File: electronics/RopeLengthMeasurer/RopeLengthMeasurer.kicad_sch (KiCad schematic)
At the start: 13 parts

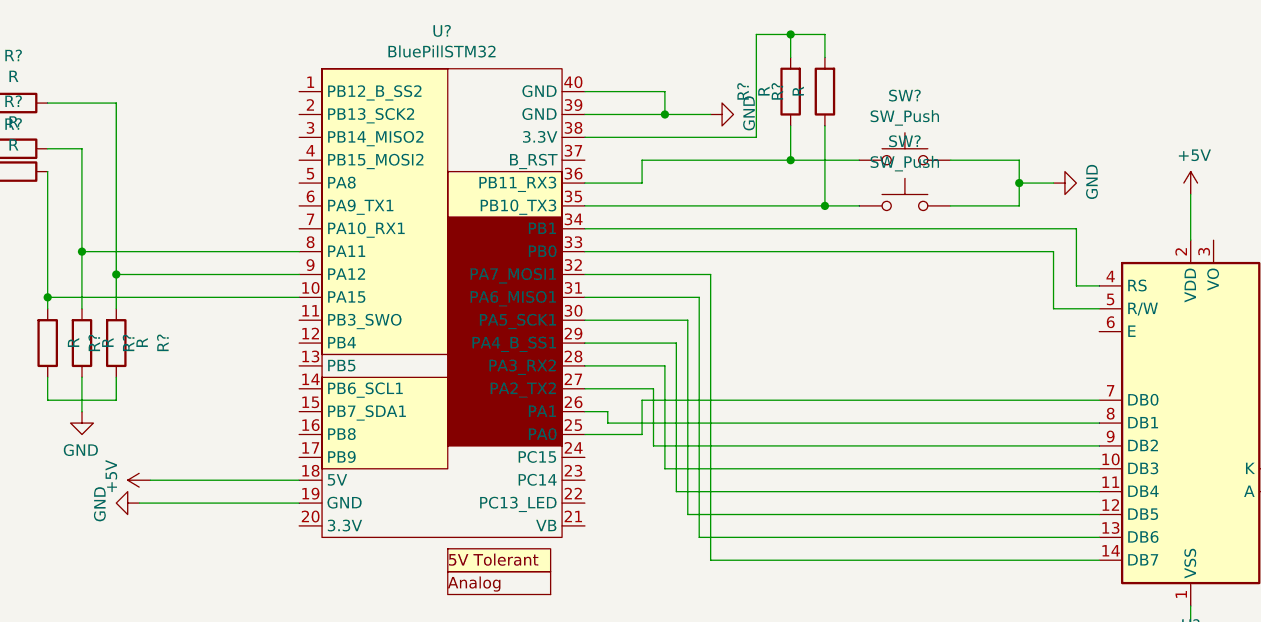
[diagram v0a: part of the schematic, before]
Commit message: Switching design to black pill.
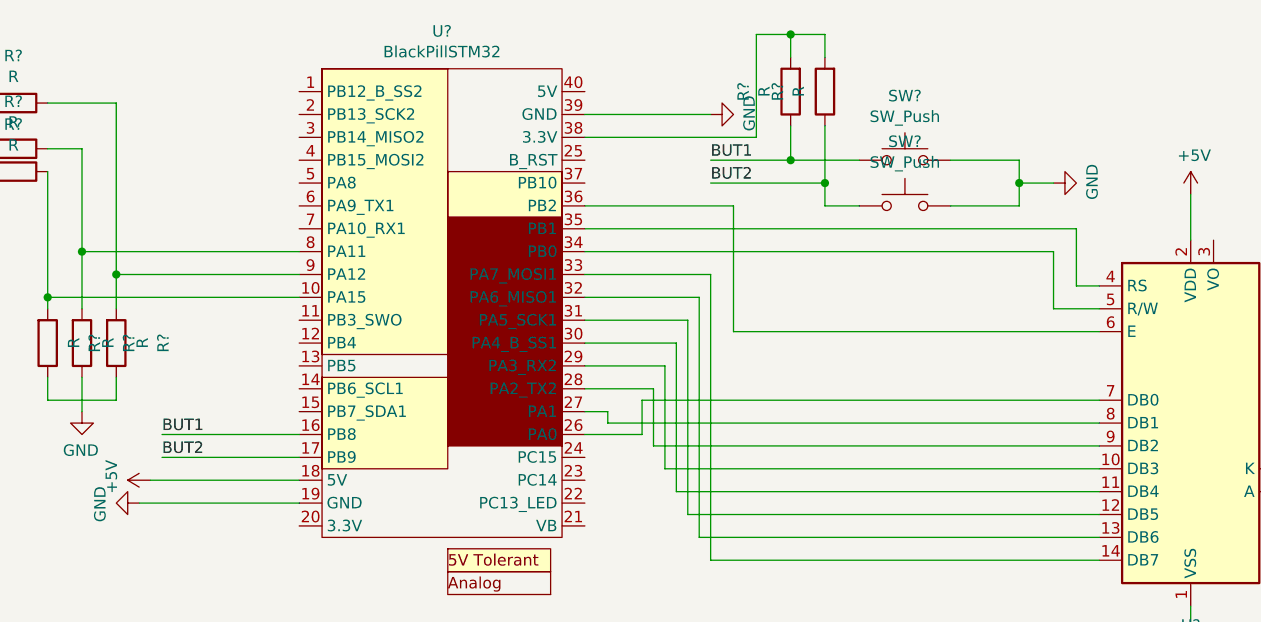
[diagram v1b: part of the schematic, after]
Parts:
- removed U?: BluePillSTM32, symbol RopeLengthMeasurerLibrary:BluePillSTM32
- added U?: BlackPillSTM32, symbol RopeLengthMeasurerLibrary:BlackPillSTM32
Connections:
- net +5V: now also U?.18 (5V)
- net GND: now also U?.19 (GND), U?.39 (GND)
- net at R?.1, R?.2: now also U?.8 (PA11)
- net at R?.1, R?.2: now also U?.10 (PA15)
- net at U?.7 (DB0): now also U?.26 (PA0)
- net at U?.8 (DB1): now also U?.27 (PA1)
- net at U?.9 (DB2): now also U?.28 (PA2_TX2)
- net at U?.10 (DB3): now also U?.29 (PA3_RX2)
- net at U?.11 (DB4): now also U?.30 (PA4_B_SS1)
- net at U?.12 (DB5): now also U?.31 (PA5_SCK1)
- net at U?.13 (DB6): now also U?.32 (PA6_MISO1)
- net at U?.14 (DB7): now also U?.33 (PA7_MOSI1)
- net at U?.5 (R/W): now also U?.34 (PB0)
- net at U?.4 (RS): now also U?.35 (PB1)
- net BUT2: now reaches R?.1, SW?.1
- net BUT2: now also U?.17 (PB9)
- net BUT1: now reaches R?.1, SW?.1
- net BUT1: now also U?.16 (PB8)
- net at R?.2, R?.2: now also U?.38 (3.3V)
- net at R?.1, R?.2: now also U?.9 (PA12)
- net at U?.6 (E): now also U?.36 (PB2)
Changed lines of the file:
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@@
     (title "Rope Length Measurer")
   )
+  (junction (at 180.34 92.71))
+  (junction (at 180.34 106.68))
   (junction (at 205.74 109.22))
-  (junction (at 184.15 111.76))
-  (junction (at 180.34 106.68))
   (junction (at 97.79 121.92))
-  (junction (at 180.34 92.71))
-  (junction (at 166.37 101.6))
   (junction (at 101.6 116.84))
   (junction (at 105.41 119.38))
+  (junction (at 184.15 109.22))
   (wire (pts (xy 81.28 110.49) (xy 78.74 110.49)))
   (wire (pts (xy 81.28 113.03) (xy 81.28 110.49)))
@@
   (wire (pts (xy 107.95 144.78) (xy 125.73 144.78)))
   (wire (pts (xy 109.22 142.24) (xy 125.73 142.24)))
-  (wire (pts (xy 157.48 99.06) (xy 166.37 99.06)))
-  (wire (pts (xy 157.48 101.6) (xy 166.37 101.6)))
+  (wire (pts (xy 110.49 137.16) (xy 125.73 137.16)))
+  (wire (pts (xy 110.49 139.7) (xy 125.73 139.7)))
+  (wire (pts (xy 157.48 101.6) (xy 171.45 101.6)))
   (wire (pts (xy 157.48 104.14) (xy 176.53 104.14)))
-  (wire (pts (xy 157.48 109.22) (xy 163.83 109.22)))
-  (wire (pts (xy 157.48 111.76) (xy 184.15 111.76)))
+  (wire (pts (xy 157.48 111.76) (xy 173.99 111.76)))
   (wire (pts (xy 157.48 114.3) (xy 212.09 114.3)))
   (wire (pts (xy 157.48 134.62) (xy 160.02 134.62)))
   (wire (pts (xy 160.02 134.62) (xy 160.02 135.89)))
   (wire (pts (xy 160.02 135.89) (xy 214.63 135.89)))
-  (wire (pts (xy 163.83 106.68) (xy 180.34 106.68)))
-  (wire (pts (xy 163.83 109.22) (xy 163.83 106.68)))
   (wire (pts (xy 163.83 133.35) (xy 163.83 137.16)))
   (wire (pts (xy 163.83 137.16) (xy 157.48 137.16)))
   (wire (pts (xy 165.1 132.08) (xy 157.48 132.08)))
   (wire (pts (xy 165.1 138.43) (xy 165.1 132.08)))
-  (wire (pts (xy 166.37 101.6) (xy 166.37 99.06)))
-  (wire (pts (xy 166.37 101.6) (xy 171.45 101.6)))
   (wire (pts (xy 166.37 129.54) (xy 157.48 129.54)))
   (wire (pts (xy 166.37 140.97) (xy 166.37 129.54)))
@@
   (wire (pts (xy 170.18 121.92) (xy 157.48 121.92)))
   (wire (pts (xy 170.18 148.59) (xy 170.18 121.92)))
+  (wire (pts (xy 171.45 106.68) (xy 180.34 106.68)))
+  (wire (pts (xy 171.45 109.22) (xy 184.15 109.22)))
   (wire (pts (xy 171.45 119.38) (xy 157.48 119.38)))
   (wire (pts (xy 171.45 151.13) (xy 171.45 119.38)))
+  (wire (pts (xy 173.99 111.76) (xy 173.99 125.73)))
+  (wire (pts (xy 173.99 125.73) (xy 214.63 125.73)))
   (wire (pts (xy 176.53 92.71) (xy 180.34 92.71)))
   (wire (pts (xy 176.53 104.14) (xy 176.53 92.71)))
@@
   (wire (pts (xy 180.34 106.68) (xy 187.96 106.68)))
   (wire (pts (xy 184.15 92.71) (xy 184.15 95.25)))
-  (wire (pts (xy 184.15 102.87) (xy 184.15 111.76)))
+  (wire (pts (xy 184.15 102.87) (xy 184.15 109.22)))
+  (wire (pts (xy 184.15 109.22) (xy 184.15 111.76)))
   (wire (pts (xy 184.15 111.76) (xy 187.96 111.76)))
   (wire (pts (xy 198.12 106.68) (xy 205.74 106.68)))
@@
   (wire (pts (xy 224.79 110.49) (xy 224.79 115.57)))
   (wire (pts (xy 224.79 156.21) (xy 224.79 161.29)))
+  (label "BUT1" (at 110.49 137.16 0)
+    (effects (font (size 1.27 1.27)) (justify left bottom))
+  )
+  (label "BUT2" (at 110.49 139.7 0)
+    (effects (font (size 1.27 1.27)) (justify left bottom))
+  )
+  (label "BUT1" (at 171.45 106.68 0)
+    (effects (font (size 1.27 1.27)) (justify left bottom))
+  )
+  (label "BUT2" (at 171.45 109.22 0)
+    (effects (font (size 1.27 1.27)) (justify left bottom))
+  )
   (symbol (lib_id "power:+5V") (at 88.9 96.52 0) (mirror y) (unit 1)
     (property "Reference" "#PWR?" (id 0) (at 88.9 100.33 0)
@@
     )
   )
-  (symbol (lib_id "RopeLengthMeasurerLibrary:BluePillSTM32") (at 140.97 125.73 0) (unit 1)
+  (symbol (lib_id "RopeLengthMeasurerLibrary:BlackPillSTM32") (at 140.97 125.73 0) (unit 1)
     (property "Reference" "U?" (id 0) (at 141.605 92.3606 0))
-    (property "Value" "BluePillSTM32" (id 1) (at 141.605 94.6593 0))
+    (property "Value" "BlackPillSTM32" (id 1) (at 141.605 94.6593 0))
     (property "Footprint" "" (id 2) (at 140.97 125.73 0)
       (effects (font (size 1.27 1.27)) hide)
@@
     (path "/7277fe0f-8eb6-42d9-9146-42338237283f" (reference "SW?") (unit 1))
     (path "/8c9fb5c0-6949-4714-a6e4-1cb24319bb3d" (reference "SW?") (unit 1))
-    (path "/363120c1-d9a0-48f5-bc66-fe3ce3559d16" (reference "U?") (unit 1))
+    (path "/3ffa81b3-2fad-40d0-843d-3ea2c963161d" (reference "U?") (unit 1))
     (path "/4f978266-5538-4d2e-ab75-02c33b1c508d" (reference "U?") (unit 1))
     (path "/91db2f3c-0f8a-4d8d-8519-75a14ded5ae0" (reference "U?") (unit 1))

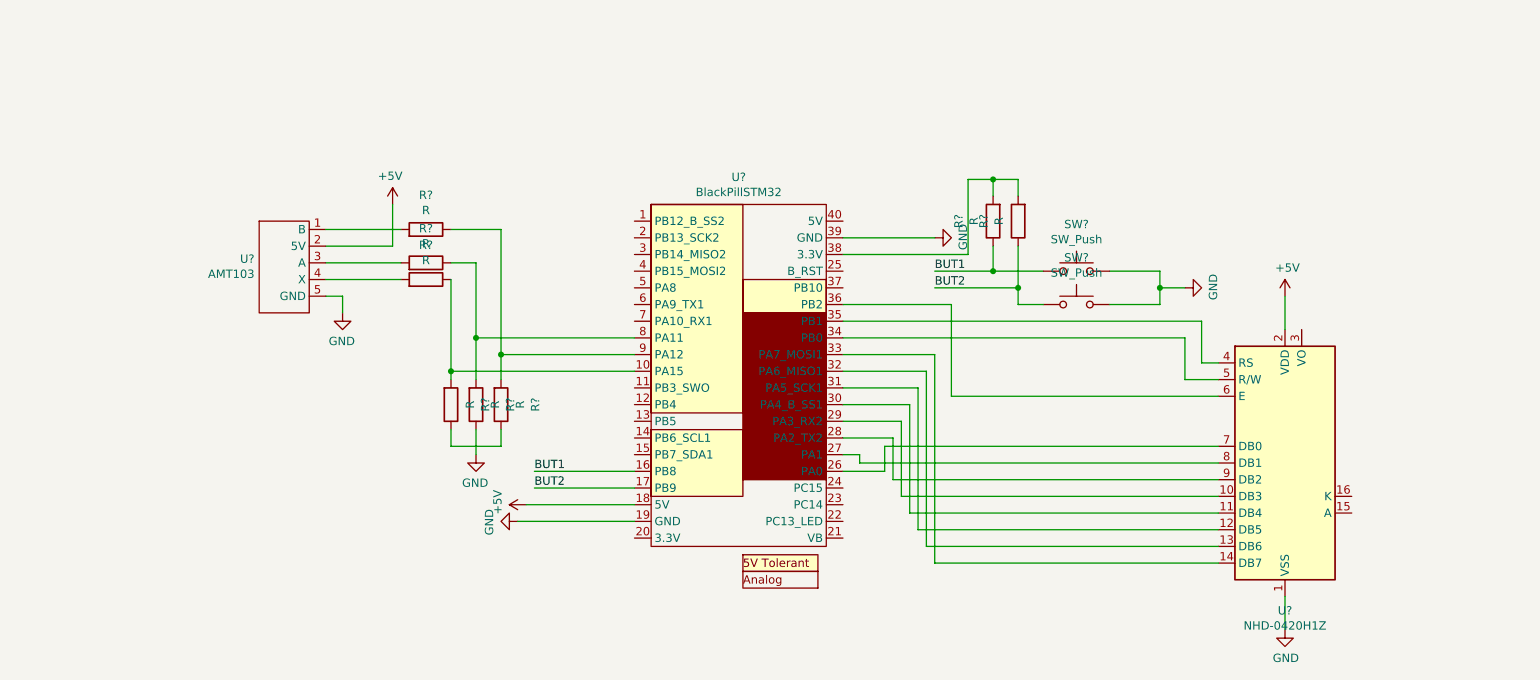
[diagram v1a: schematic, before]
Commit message: Software working with new circuit board. Reset button also working.
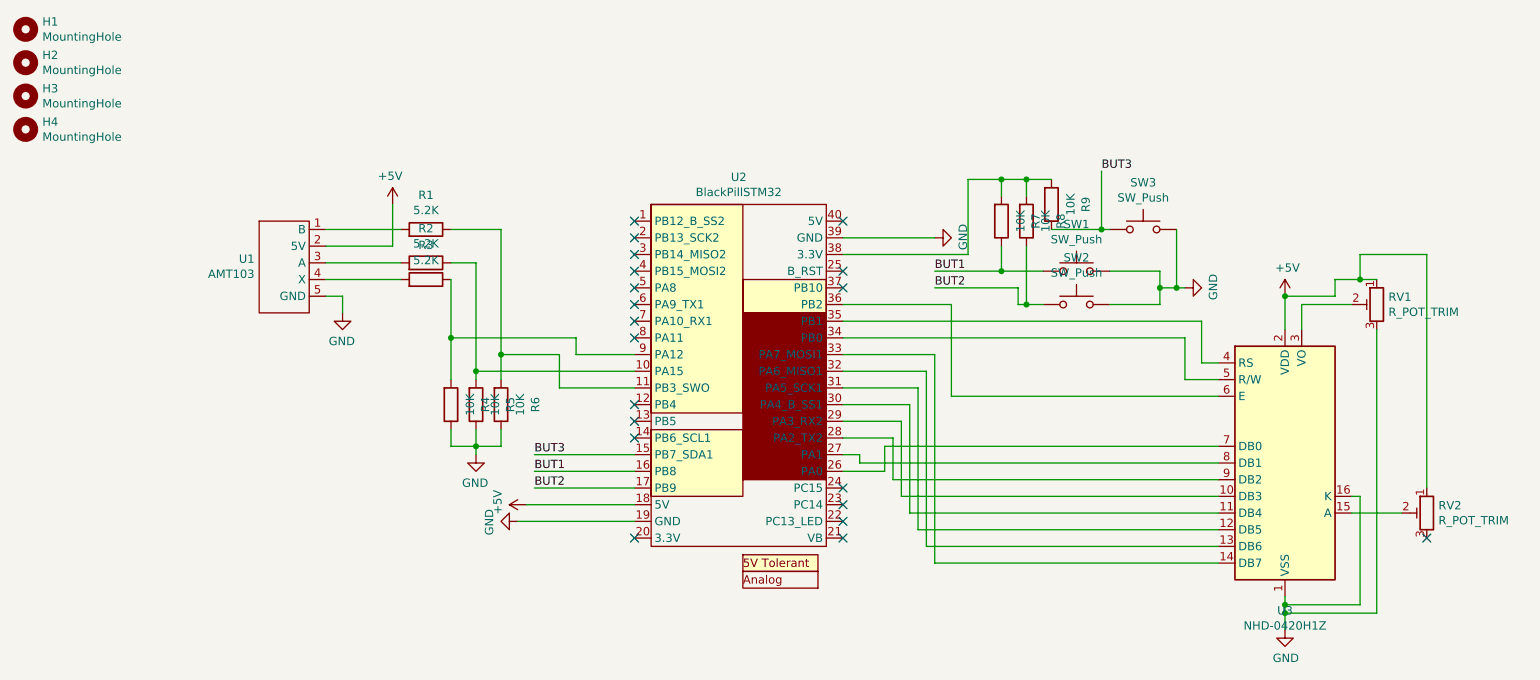
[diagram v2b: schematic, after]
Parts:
- removed R? (x6): R, symbol RopeLengthMeasurerLibrary:R
- removed SW? (x2): SW_Push, symbol RopeLengthMeasurerLibrary:SW_Push
- added H1, H2, H3, H4: MountingHole, MountingHole:MountingHole_3.2mm_M3, symbol Mechanical:MountingHole
- added R2, R3: 5.2K, Resistor_SMD:R_0603_1608Metric_Pad1.05x0.95mm_HandSolder, symbol RopeLengthMeasurerLibrary:R
- added R5, R6, R7, R8, R9: 10K, Resistor_SMD:R_0603_1608Metric_Pad1.05x0.95mm_HandSolder, symbol RopeLengthMeasurerLibrary:R
- added RV1, RV2: R_POT_TRIM, Potentiometer_THT:Potentiometer_Piher_PT-10-V10_Vertical, symbol Device:R_POT_TRIM
- added SW1, SW2, SW3: SW_Push, Button_Switch_THT:SW_PUSH_6mm_H5mm, symbol RopeLengthMeasurerLibrary:SW_Push
- R1: renamed from R?; value R -> 5.2K; footprint (none) -> Resistor_SMD:R_0603_1608Metric_Pad1.05x0.95mm_HandSolder; Supplier (none) -> Digikey; Supplier # (none) -> 1276-5086-1-ND
- R4: renamed from R?; value R -> 10K; footprint (none) -> Resistor_SMD:R_0603_1608Metric_Pad1.05x0.95mm_HandSolder
- U1: renamed from U?; footprint (none) -> Connector_PinHeader_2.54mm:PinHeader_1x05_P2.54mm_Vertical
- U2: renamed from U?; footprint (none) -> RopeLengthMeasurer:BlackPill; Supplier (none) -> Amazon
- U3: renamed from U?; footprint Display:NHD-0420H1Z -> Display:WC1602A; Supplier (none) -> Digikey; Supplier # (none) -> NHD-0216K1Z-FL-YBW-ND
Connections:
- net +5V: now also RV1.1, RV2.1
- net BUT1: now also R7.1, SW1.1
- net BUT2: now also R8.1, SW2.1
- net GND: now also R4.1, U3.16 (K), R5.1, R6.1, RV1.3, SW1.2, SW2.2, SW3.2
- net at U1.3 (A): now also R2.2
- net at U2.10 (PA15): now also R2.1, R5.2; no longer R4.2
- net at U2.11 (PB3_SWO): now also R1.1, R6.2
- net BUT3: now reaches U2.15 (PB7_SDA1)
- net BUT3: now also R9.1, SW3.1
- net at U2.38 (3.3V): now also R7.2, R8.2, R9.2
- net at U2.9 (PA12): now also R4.2, R3.1; no longer R1.1
- net at U1.4 (X): now also R3.2
- net at U3.15 (A): now also RV2.2
- net at U3.3 (VO): now also RV1.2
- no-connect marks 0 -> 20
